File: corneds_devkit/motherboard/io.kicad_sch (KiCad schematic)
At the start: 26 parts, among them J1 Conn_01x14_Male, J10 USB-C_2.0_R, J2 Conn_01x14_Male, J3 Conn_01x14_Male, J4 Conn_01x14_Male, J9 USB-C_2.0_L

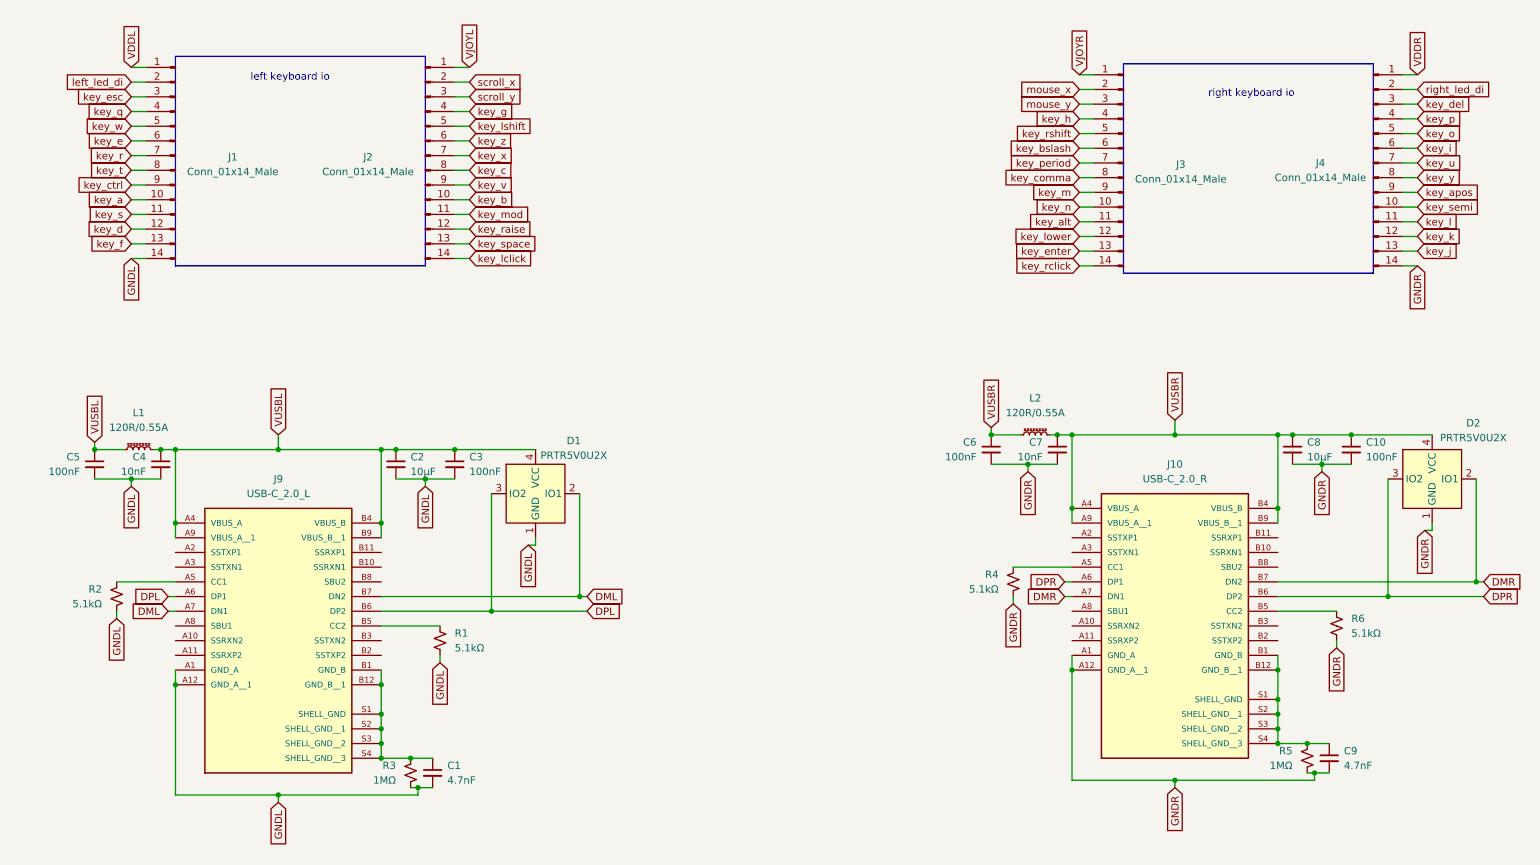
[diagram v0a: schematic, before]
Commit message: ordered devkit rev A
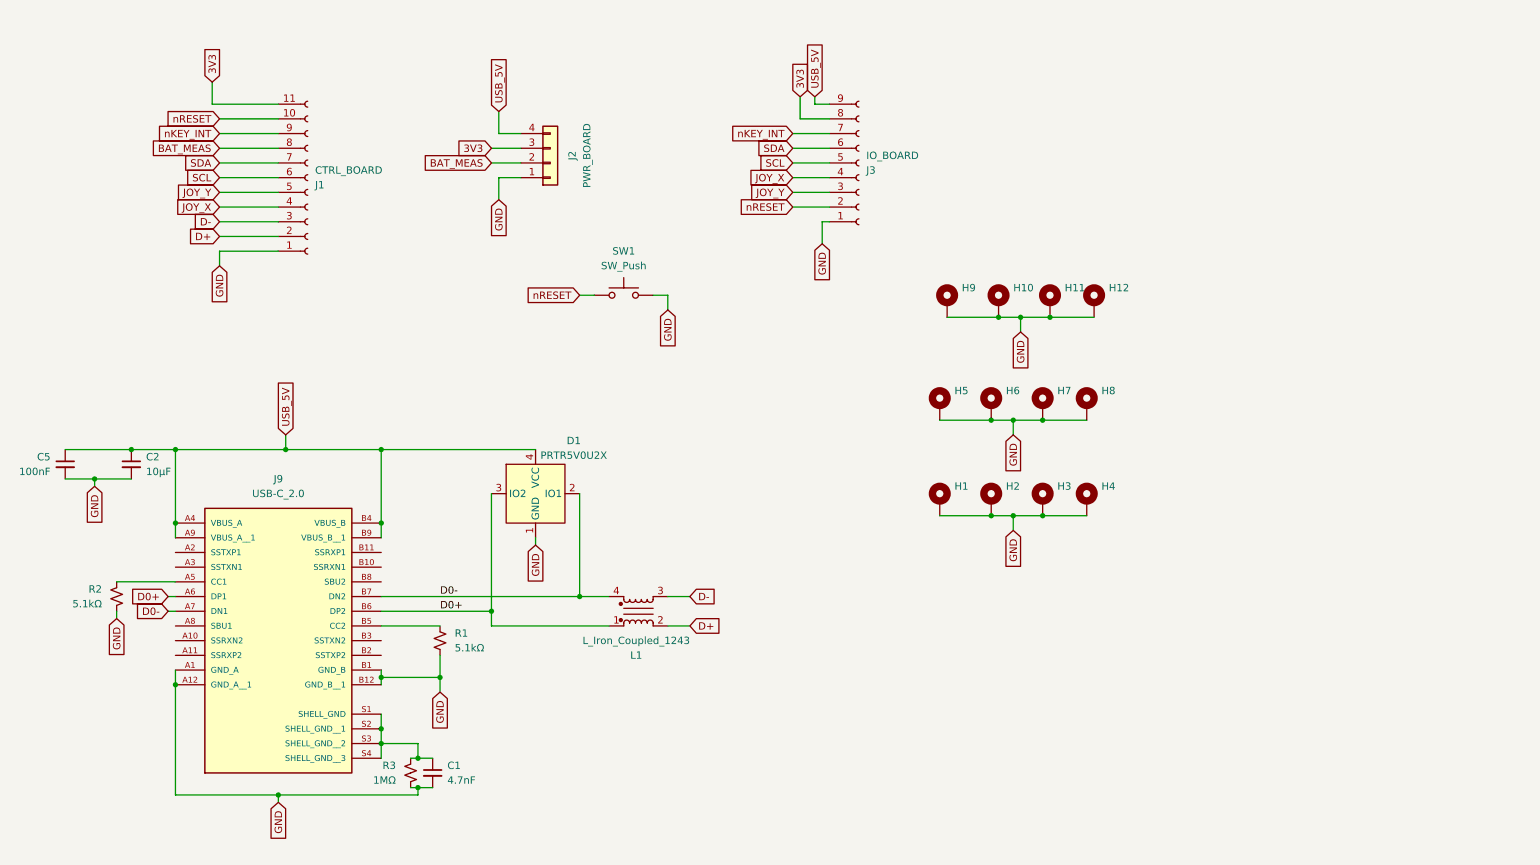
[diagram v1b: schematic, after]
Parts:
- removed C10, C3, C6: 100nF, symbol Device:C_Small
- removed C4, C7: 10nF, symbol Device:C_Small
- removed C8: 10μF, symbol Device:C_Small
- removed C9: 4.7nF, symbol Device:C_Small
- removed D2: PRTR5V0U2X, symbol entropy:PRTR5V0U2X
- removed J1, J2, J3, J4: Conn_01x14_Male, symbol Connector:Conn_01x14_Male
- removed J10: USB-C_2.0_R, USB4056-03-A_REVA2:GCT_USB4056-03-A_REVA2, symbol usb-c:USB4056-03-A_REVA2
- removed L1, L2: 120R/0.55A, symbol Device:L_Ferrite_Small
- removed R4, R6: 5.1kΩ, symbol Device:R_Small_US
- removed R5: 1MΩ, symbol Device:R_Small_US
- added H1, H10, H11, H12, H2, H3, H4, H5, H6, H7, H8, H9: ~, MountingHole:MountingHole_3.2mm_M3_Pad_Via, symbol Mechanical:MountingHole_Pad
- added J1: CTRL_BOARD, Connector_PinHeader_1.27mm:PinHeader_1x11_P1.27mm_Vertical, symbol Connector:Conn_01x11_Socket
- added J2: PWR_BOARD, Connector_PinHeader_1.27mm:PinHeader_1x04_P1.27mm_Vertical, symbol Connector_Generic:Conn_01x04
- added J3: IO_BOARD, Connector_PinHeader_1.27mm:PinHeader_1x09_P1.27mm_Vertical, symbol Connector:Conn_01x09_Socket
- added L1: L_Iron_Coupled_1243, Inductor_SMD:L_CommonModeChoke_Coilcraft_0603USB, symbol Device:L_Iron_Coupled_1243
- added SW1: SW_Push, Button_Switch_SMD:SW_Tactile_SPST_NO_Straight_CK_PTS636Sx25SMTRLFS, symbol Switch:SW_Push
- C1: footprint (none) -> Capacitor_SMD:C_0603_1608Metric
- C2, C5: footprint (none) -> Capacitor_SMD:C_0402_1005Metric
- D1: footprint (none) -> Package_TO_SOT_SMD:SOT-143
- J9: value USB-C_2.0_L -> USB-C_2.0; footprint USB4056-03-A_REVA2:GCT_USB4056-03-A_REVA2 -> Connector_USB:USB_C_Receptacle_GCT_USB4110
- R1, R2, R3: footprint (none) -> Resistor_SMD:R_0402_1005Metric
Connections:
- net at C1.1, J9.S1 (SHELL_GND), J9.S2 (SHELL_GND__1)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: no longer J9.B1 (GND_B), J9.B12 (GND_B__1)
- net DML renamed D0-
- net D0-: now also L1.4
- net DPL renamed D0+
- net D0+: now also L1.1
- net GNDL renamed GND
- net GND: now also J9.B1 (GND_B), J9.B12 (GND_B__1), H1.1, H10.1, H11.1, H12.1, H2.1, H3.1, H4.1, H5.1, H6.1, H7.1, H8.1, H9.1, J1.1 (Pin_1), J2.1 (Pin_1), J3.1 (Pin_1), SW1.2
- net VUSBL renamed USB_5V
- net USB_5V: now also J2.4 (Pin_4), J3.9 (Pin_9)
- new net 3V3: J1.11 (Pin_11), J2.3 (Pin_3), J3.8 (Pin_8)
- new net BAT_MEAS: J1.8 (Pin_8), J2.2 (Pin_2)
- new net D+: J1.2 (Pin_2), L1.2
- new net D-: J1.3 (Pin_3), L1.3
- new net JOY_X: J1.4 (Pin_4), J3.4 (Pin_4)
- new net JOY_Y: J1.5 (Pin_5), J3.3 (Pin_3)
- new net SCL: J1.6 (Pin_6), J3.5 (Pin_5)
- new net SDA: J1.7 (Pin_7), J3.6 (Pin_6)
- new net nKEY_INT: J1.9 (Pin_9), J3.7 (Pin_7)
- new net nRESET: J1.10 (Pin_10), J3.2 (Pin_2), SW1.1
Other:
- note removed: "left keyboard io"
- note removed: "right keyboard io"
- moved on the sheet: C2, C5
